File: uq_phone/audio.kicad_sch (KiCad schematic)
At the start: 34 parts, among them J10 Conn_01x02, J9 SJ-3551B-MSMT-TR-67, U10 TS3A5018RSVR, U11 NAU88C22YG

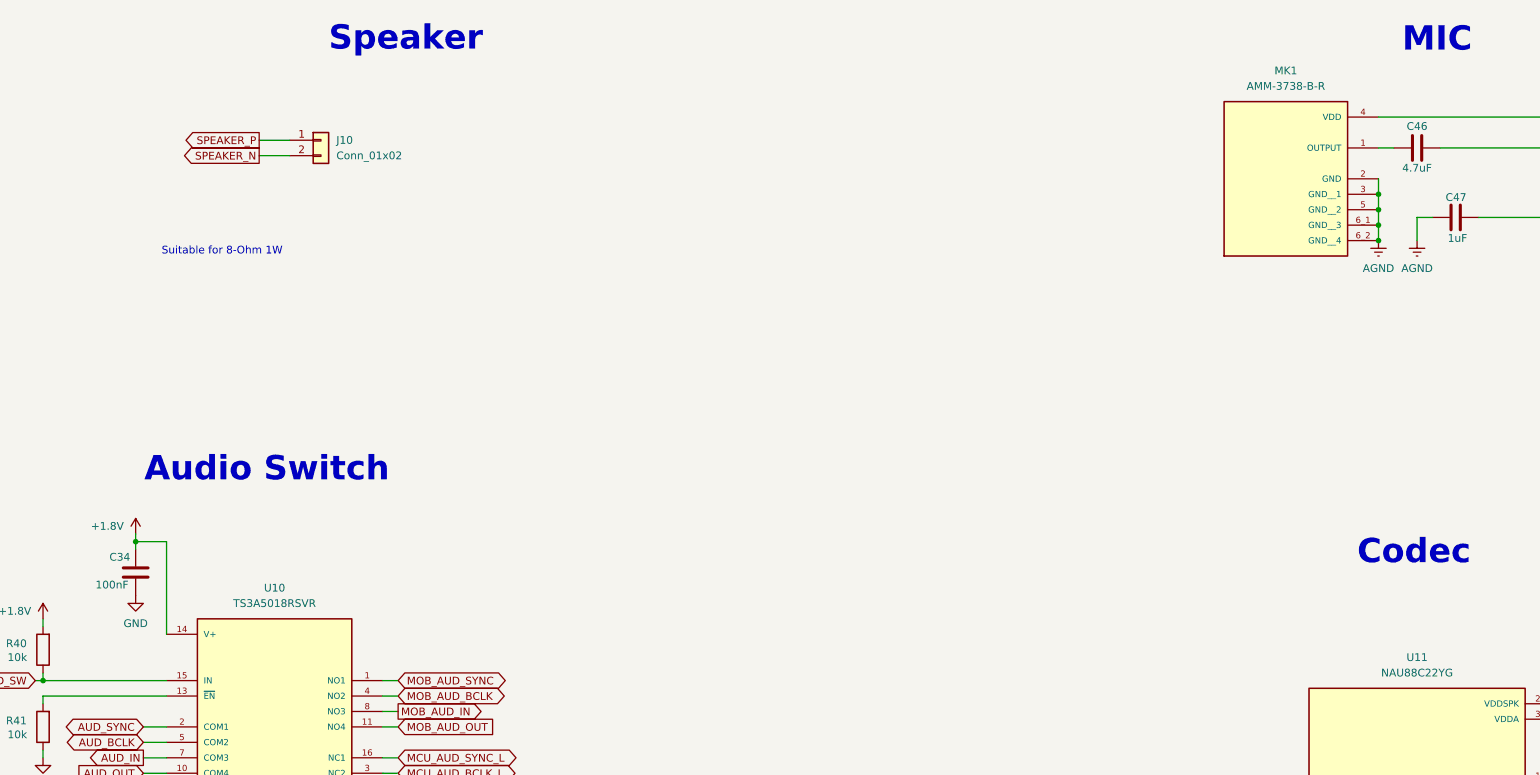
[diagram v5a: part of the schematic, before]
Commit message: Add LEDs, Inital Buttons
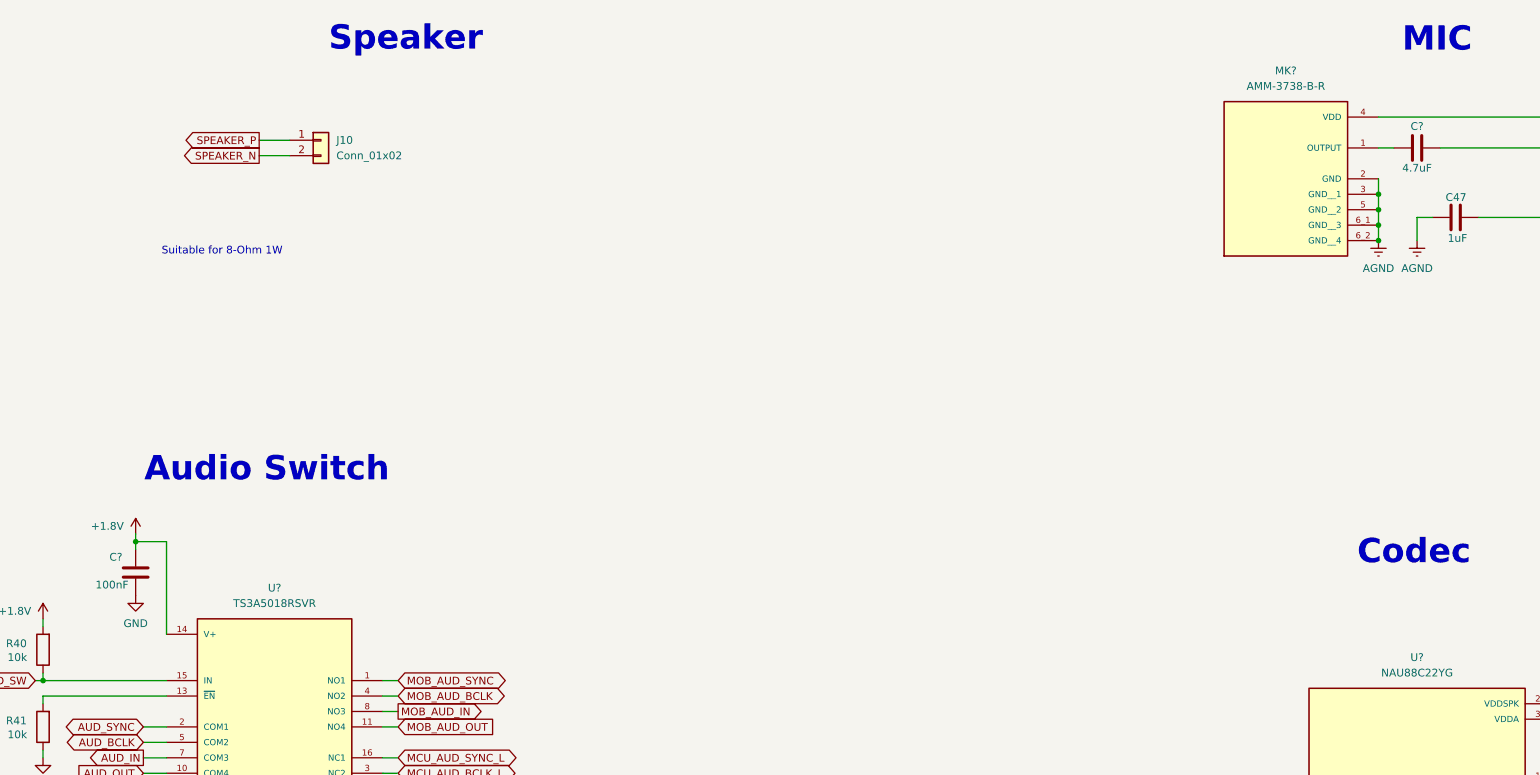
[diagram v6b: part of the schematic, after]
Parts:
- renumbered C46 to C?, C34 to C?, MK1 to MK?, U10 to U?, U11 to U?
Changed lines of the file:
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@@
 		(on_board yes)
 		(dnp no)
-		(property "Reference" "C46"
+		(property "Reference" "C?"
 			(at 267.97 44.704 90)
 			(effects
@@
 		)
 		(instances
-			(project ""
+			(project "uq_phone"
 				(path "/14f57415-6807-40a5-bb38-3cb818a2cdae/e19f4f8c-44cb-4a36-b4d3-60ff6ff42a2f"
-					(reference "C46")
+					(reference "C?")
 					(unit 1)
 				)
@@
 		(dnp no)
 		(fields_autoplaced yes)
-		(property "Reference" "MK1"
+		(property "Reference" "MK?"
 			(at 246.38 35.56 0)
 			(effects
@@
 		)
 		(instances
-			(project ""
+			(project "uq_phone"
 				(path "/14f57415-6807-40a5-bb38-3cb818a2cdae/e19f4f8c-44cb-4a36-b4d3-60ff6ff42a2f"
-					(reference "MK1")
+					(reference "MK?")
 					(unit 1)
 				)
@@
 		(on_board yes)
 		(dnp no)
-		(property "Reference" "C34"
+		(property "Reference" "C?"
 			(at 52.832 115.57 0)
 			(effects
@@
 		)
 		(instances
-			(project ""
+			(project "uq_phone"
 				(path "/14f57415-6807-40a5-bb38-3cb818a2cdae/e19f4f8c-44cb-4a36-b4d3-60ff6ff42a2f"
-					(reference "C34")
+					(reference "C?")
 					(unit 1)
 				)
@@
 		(dnp no)
 		(fields_autoplaced yes)
-		(property "Reference" "U10"
+		(property "Reference" "U?"
 			(at 80.01 120.65 0)
 			(effects
@@
 		)
 		(instances
-			(project ""
+			(project "uq_phone"
 				(path "/14f57415-6807-40a5-bb38-3cb818a2cdae/e19f4f8c-44cb-4a36-b4d3-60ff6ff42a2f"
-					(reference "U10")
+					(reference "U?")
 					(unit 1)
 				)
@@
 		(dnp no)
 		(fields_autoplaced yes)
-		(property "Reference" "U11"
+		(property "Reference" "U?"
 			(at 267.97 132.08 0)
 			(effects
@@
 		)
 		(instances
-			(project ""
+			(project "uq_phone"
 				(path "/14f57415-6807-40a5-bb38-3cb818a2cdae/e19f4f8c-44cb-4a36-b4d3-60ff6ff42a2f"
-					(reference "U11")
+					(reference "U?")
 					(unit 1)
 				)

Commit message: Routing Init
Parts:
- gave numbers to parts that had none: 5
- renumbered C35 to C37, C36 to C38, C37 to C39, C38 to C40, C39 to C41, C47 to C43, C40 to C44, C41 to C45, C42 to C46, C43 to C47, C44 to C48, C45 to C49, J9 to J10, J10 to J11, R40 to R35, R41 to R36, R42 to R37, R47 to R38, R48 to R39, R43 to R40, R44 to R41, R45 to R42, R46 to R43, R49 to R44, R50 to R45, R51 to R46, R54 to R47
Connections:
- net AUD_SW renamed AUD_SW_L
- net MCU_AUD_IN: no longer names the net of U13.9 (NC3)
- no-connect marks 6 -> 7
